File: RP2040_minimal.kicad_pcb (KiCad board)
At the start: 4 copper layers, 38.1 x 50.8 mm, 37 parts, among them J1 Conn_02x05_Odd_Even, J2 Conn_01x02, J3 Conn_01x02, U1 LM4040DBZ-3, U2 W25Q128JVS, U3 RP2040, U4 LM4040DBZ-3, Y1 ABLS-12.000MHZ-B4-T, Y2 X322516MLB4SI

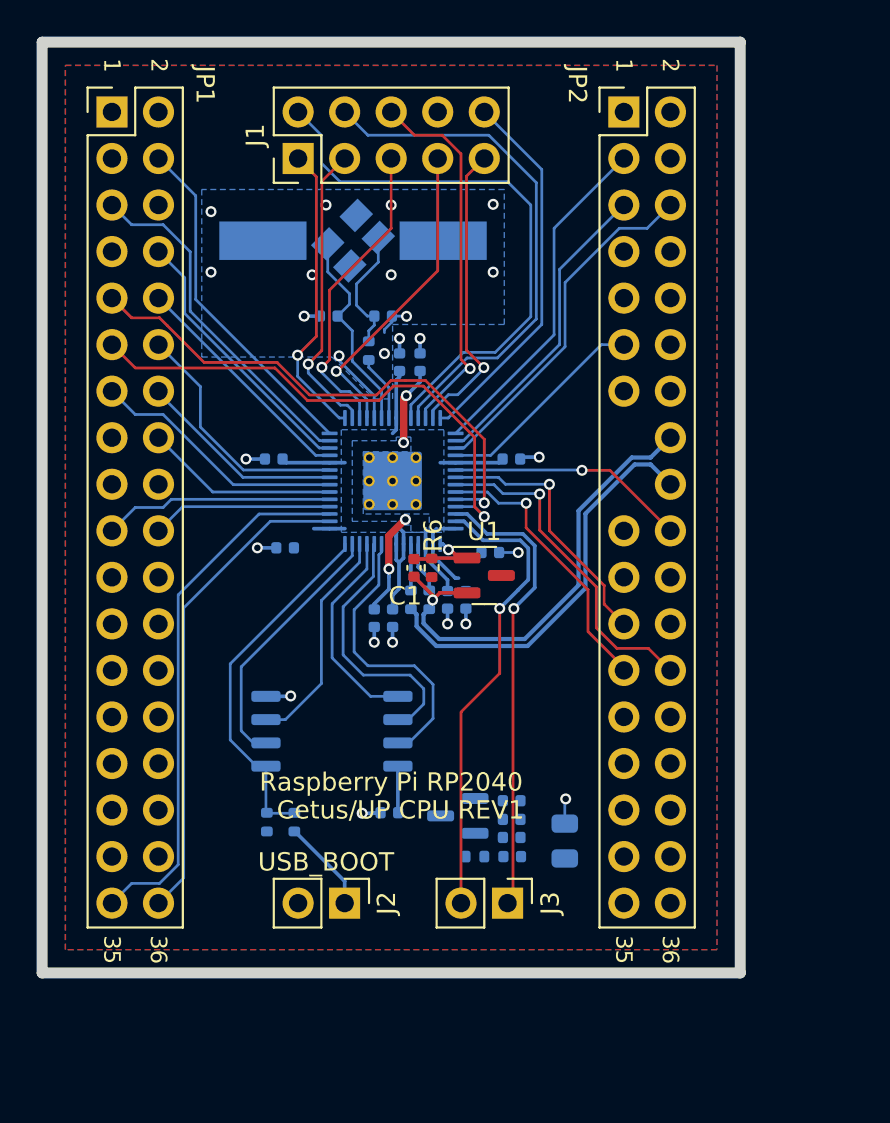
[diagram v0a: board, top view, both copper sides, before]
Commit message: Board ready for production, tab on bottom
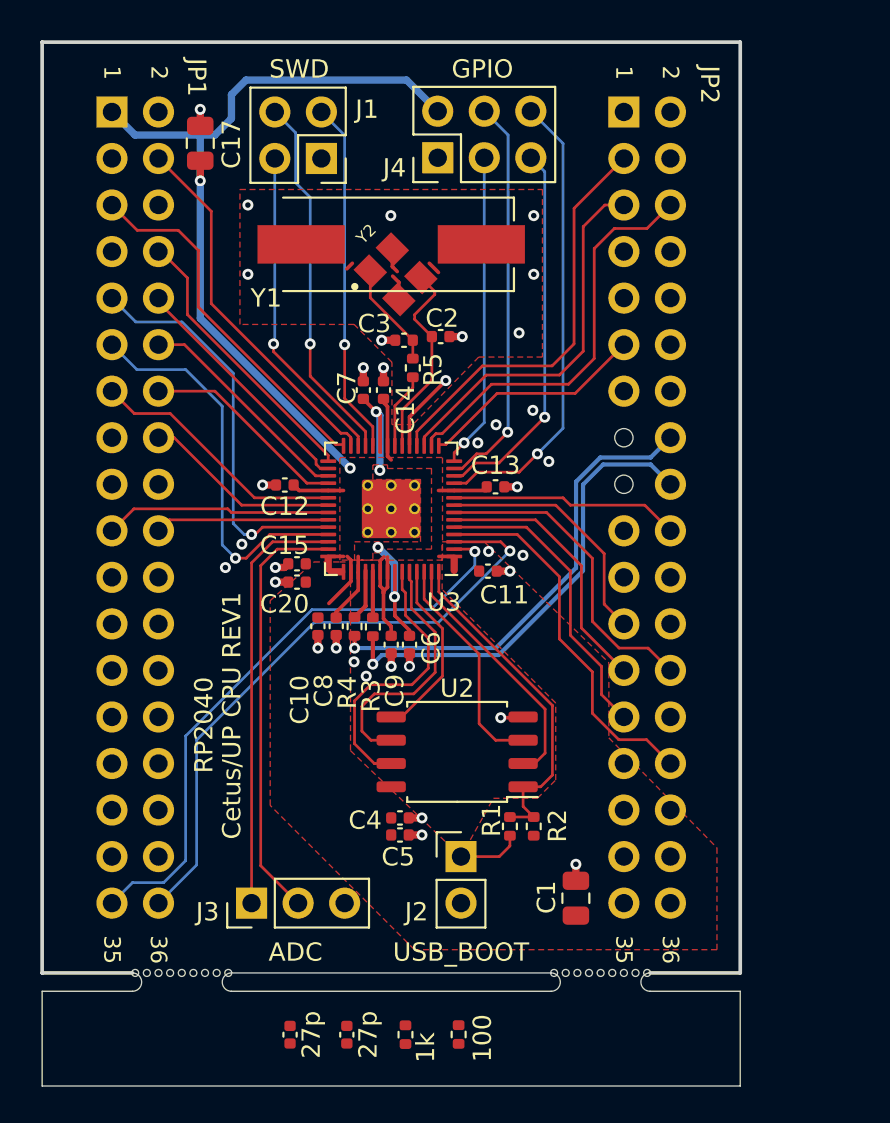
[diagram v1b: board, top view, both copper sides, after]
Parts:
- removed C19: 27p, Capacitor_SMD:C_0402_1005Metric
- removed U1, U4: LM4040DBZ-3, Package_TO_SOT_SMD:SOT-23
- added C20: 100n, Capacitor_SMD:C_0402_1005Metric, F.Cu at (154.9, 104.4)
- added J4: Conn_02x03_Odd_Even, Connector_PinHeader_2.54mm:PinHeader_2x03_P2.54mm_Vertical, F.Cu at (162.6, 81.2)
- added mouse-bite-2mm-slot: VAL**, RP2040_minimal:mouse-bite-1mm-slot_singlesided, F.Cu at (148.6, 126.2)
- added mouse-bite-2mm-slot: VAL**, RP2040_minimal:mouse-bite-1mm-slot_singlesided, F.Cu at (171.4, 126.2)
- C1: value 2.2u -> 47u; footprint Capacitor_SMD:C_0402_1005Metric -> Capacitor_SMD:C_0805_2012Metric
- C10, C8: value 1u -> 2.2u; moved to F.Cu
- C11, C12, C13, C14, C15, C16, C18, C4, C5, C6, C7, C9, R1, R2, R3, R4, U2, U3, Y1, Y2: moved to F.Cu
- C17: value 10u -> 47u; moved to F.Cu
- C2, C3: value 27p -> 30p; moved to F.Cu
- J1: value Conn_02x05_Odd_Even -> Conn_01x03; footprint Connector_PinHeader_2.54mm:PinHeader_2x05_P2.54mm_Vertical -> Connector_PinHeader_2.54mm:PinHeader_2x02_P2.54mm_Vertical
- J3: footprint Connector_PinHeader_2.54mm:PinHeader_1x02_P2.54mm_Vertical -> Connector_PinHeader_2.54mm:PinHeader_1x03_P2.54mm_Vertical
- JP1: footprint Connector_PinHeader_2.54mm:PinHeader_2x18_P2.54mm_Vertical -> RP2040_minimal:PinHeader_2x18_P2.54mm_Vertical_backside; moved to B.Cu
- JP2: footprint Connector_PinHeader_2.54mm:PinHeader_2x18_P2.54mm_Vertical -> RP2040_minimal:PinHeader_2x18_P2.54mm_Vertical_backside_pads15+17_removed; moved to B.Cu
- R5: value 1k -> 470; moved to F.Cu
- R6: value 200 -> 100
- R7: value 200 -> 1k; moved to F.Cu
- moved C17 43.0 mm to (149.6, 80.5)
- moved R6 25.5 mm to (163.7, 129.1), turned to -90 degrees
- moved C1 20.1 mm to (170.1, 121.7), turned to 90 degrees
- moved C16 16.9 mm to (154.5, 129.1), turned to 90 degrees
- moved R2 14.6 mm to (167.8, 117.7)
- moved C18 14.0 mm to (157.6, 129.1), turned to 90 degrees
- moved J3 14.0 mm to (152.4, 121.9), turned to 90 degrees
- moved C12 12.4 mm to (154.2, 99.1), turned to 180 degrees
- moved C13 12.2 mm to (165.7, 99.2), turned to 0 degrees
- moved R1 11.8 mm to (166.5, 117.7)
- moved C11 11.1 mm to (165.3, 103.8), turned to 0 degrees
- moved C15 10.6 mm to (154.9, 103.4), turned to 180 degrees
- moved R7 10.4 mm to (160.8, 129.1), turned to -90 degrees
- moved C10 8.20 mm to (156.0, 106.8)
- moved U2 6.93 mm to (163.6, 113.7), turned to 180 degrees
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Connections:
- C1 pad 1: /ADC_AVDD -> +3V3
- C4 pad 1: unconnected-(C4-Pad1) -> +3V3
- C4 pad 2: unconnected-(C4-Pad2) -> GND
- J1 pad 1: /GPIO12 -> GND
- J1 pad 2: /SWCLK -> /RUN
- J1 pad 3: /GPIO13 -> /SWCLK
- JP1 pad 1: /AVCC -> +3V3
- JP1 pad 2: /AGND -> GND
- JP2 pad 27: unconnected-(JP2-Pin_27-Pad27) -> /BTN
- JP2 pad 3: /LIMIT_Y -> /LIM_Y
- JP2 pad 30: unconnected-(JP2-Pin_30-Pad30) -> /INP
- JP2 pad 36: /VCC -> +3V3
- R6 pad 1: +3V3 -> unconnected-(R6-Pad1)
- R6 pad 2: /ADC_AVDD -> unconnected-(R6-Pad2)
- U3 pad 11: /AMP_MOD1 -> /GPIO5
- U3 pad 12: /LED -> /GPIO4
- U3 pad 13: /BUZZER -> /GPIO3
- U3 pad 14: /DOOR -> /GPIO2
- U3 pad 15: /GPIO12 -> /LIGHT
- U3 pad 16: /GPIO13 -> /DIR_Y
- U3 pad 17: /GPIO14 -> /STEP_Y
- U3 pad 18: /GPIO15 -> /LIM_Y
- U3 pad 2: /STEP_E -> /DIR_E
- U3 pad 27: /GPIO16 -> /DOOR
- U3 pad 28: /GPIO17 -> /BUZZER
- U3 pad 29: /LIMIT_Y -> /LED
- U3 pad 3: /DIR_E -> /STEP_E
- U3 pad 30: /STEP_Y -> /AMP_MOD1
- U3 pad 31: /DIR_Y -> /AMP_MOD2
- U3 pad 32: /LIGHT -> /EXT_HEAT
- U3 pad 34: /LIM_X -> /MOTOR_PWR
- U3 pad 35: /LIM_Z -> /BED_HEAT
- U3 pad 36: /DIR_Z -> /DIR_X
- U3 pad 37: /STEP_Z -> /STEP_X
- U3 pad 4: /STEP_X -> /INP
- U3 pad 43: /ADC_AVDD -> +3V3
- U3 pad 5: /DIR_X -> /BTN
- U3 pad 6: /BED_HEAT -> /STEP_Z
- U3 pad 7: /MOTOR_PWR -> /DIR_Z
- U3 pad 8: /EXT_HEAT -> /LIM_Z
- U3 pad 9: /AMP_MOD2 -> /LIM_X
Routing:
- net +3V3: track 26.1 -> 66.3 mm, vias 0 -> 2
- net /GPIO5: track 0.00 -> 25.2 mm, vias 0 -> 1
- net /LIM_Y: track 0.00 -> 22.5 mm
- net /GPIO3: track 0.00 -> 21.8 mm, vias 0 -> 1
- net /GPIO4: track 0.00 -> 20.7 mm, vias 0 -> 1
- net /GPIO17: track 20.6 -> 0.00 mm
- net /INP: track 0.00 -> 20.3 mm
- net /LIMIT_Y: track 18.8 -> 0.00 mm
- net /GPIO15: track 17.3 -> 0.00 mm, vias 1 -> 0
- net /GPIO2: track 0.00 -> 17.2 mm, vias 0 -> 1
- net /GPIO14: track 16.9 -> 0.00 mm, vias 1 -> 0
- net /BTN: track 0.00 -> 16.5 mm
- net /GPIO16: track 16.4 -> 0.00 mm, vias 1 -> 0
- net /GPIO12: track 16.3 -> 0.00 mm, vias 1 -> 0
- net /GPIO13: track 16.2 -> 0.00 mm, vias 1 -> 0
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- added copper zone on F.Cu, net +1V1
- added copper zone on F.Cu, net GND
- removed copper zone on B.Cu, net +1V1
- removed copper zone on B.Cu, net +3V3
- removed copper zone on B.Cu, net GND
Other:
- board size 38.1 x 50.8 mm -> 38.1 x 57 mm
- rule pad_to_mask_clearance: 0.051 -> 0
- board text added: "ADC"
- board text added: "GPIO"
- board text added: "RP2040"
- board text added: "SWD"
- board text removed: "Raspberry Pi RP2040"

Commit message: First production batch sent to JLCPCB
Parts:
- moved R6 39.9 mm to (182.7, 94.0), turned to 90 degrees
- moved mouse-bite-2mm-slot 39.4 mm to (179.6, 87.6), turned to 90 degrees
- moved R7 37.8 mm to (182.7, 98.3), turned to 90 degrees
- moved C18 37.2 mm to (182.7, 101.6), turned to -90 degrees
- moved C16 36.9 mm to (182.7, 105.3), turned to -90 degrees
- moved mouse-bite-2mm-slot 34.2 mm to (179.6, 111.8), turned to 90 degrees
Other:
- board size 38.1 x 57 mm -> 44.3 x 50.8 mm
